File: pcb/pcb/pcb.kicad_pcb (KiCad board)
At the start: 2 copper layers, 66 x 40.6 mm, 14 parts, among them J1 UART, J2 Barrel_Jack, J3 Stepper, U1 ESP32-WROOM-32, U2 TSR_1-2433

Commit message: Route pcb
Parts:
- added H1: MountingHole, MountingHole:MountingHole_2.7mm_M2.5_Pad, F.Cu at (182.9, 76.2)
- added H2: MountingHole, MountingHole:MountingHole_2.5mm_Pad, F.Cu at (241.3, 76.2)
- added H3: MountingHole, MountingHole:MountingHole_2.5mm_Pad, F.Cu at (182.9, 109.2)
- added H4: MountingHole, MountingHole:MountingHole_2.5mm_Pad, F.Cu at (241.3, 109.2)
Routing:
- net GND: track 0.00 -> 148.7 mm
- net +12V: track 0.00 -> 50.2 mm
- net +3V3: track 0.00 -> 46.0 mm, vias 0 -> 1
- net /SLP: track 0.00 -> 44.2 mm
- net /DIR: track 0.00 -> 40.8 mm
- net /STEP: track 0.00 -> 38.8 mm
- net Net-(C1-Pad1): track 0.00 -> 34.1 mm, vias 0 -> 2
- net /B2: track 0.00 -> 31.7 mm
- net /B1: track 0.00 -> 31.7 mm
- net /A1: track 0.00 -> 31.0 mm
- net /A2: track 0.00 -> 30.2 mm
- net /RX: track 0.00 -> 17.2 mm
- net /TX: track 0.00 -> 8.45 mm
- net Net-(C6-Pad1): track 0.00 -> 6.42 mm
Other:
- outline, holes or cut-outs redrawn

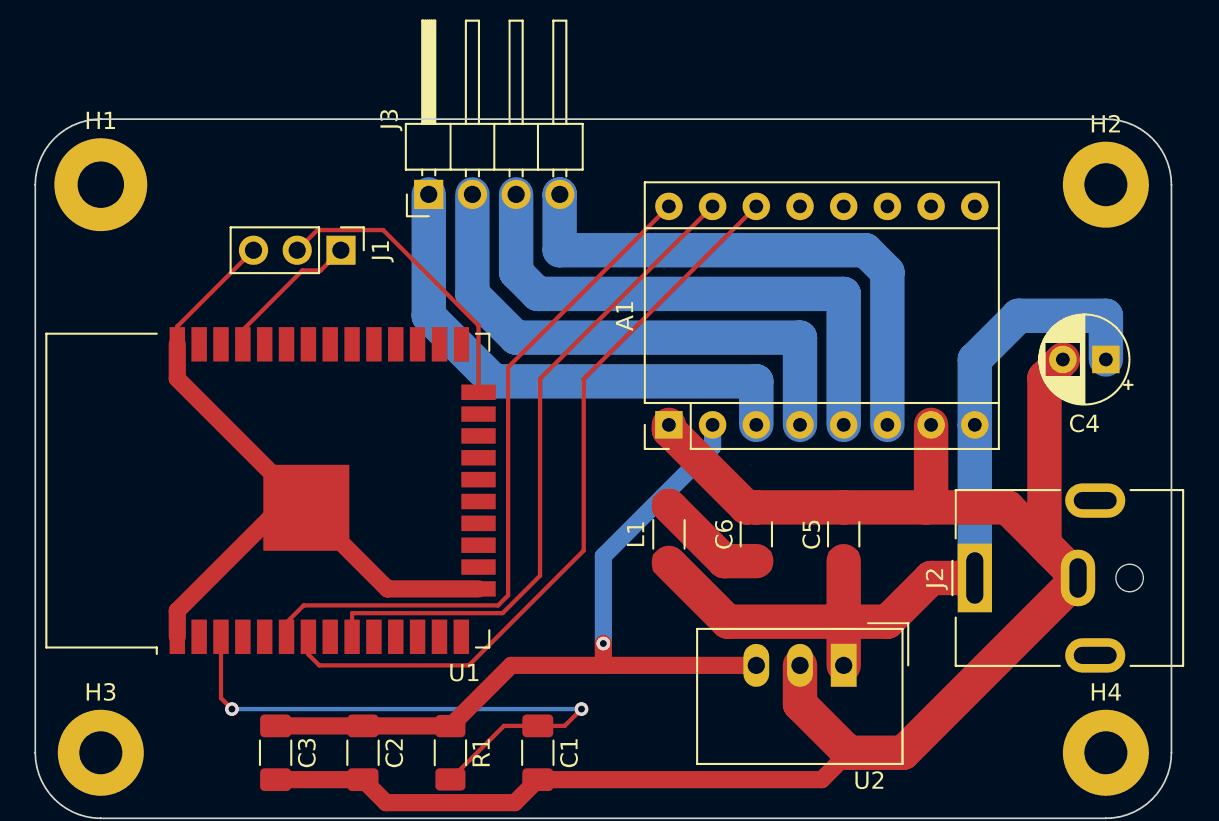
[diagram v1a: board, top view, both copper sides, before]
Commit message: Add silkscreen
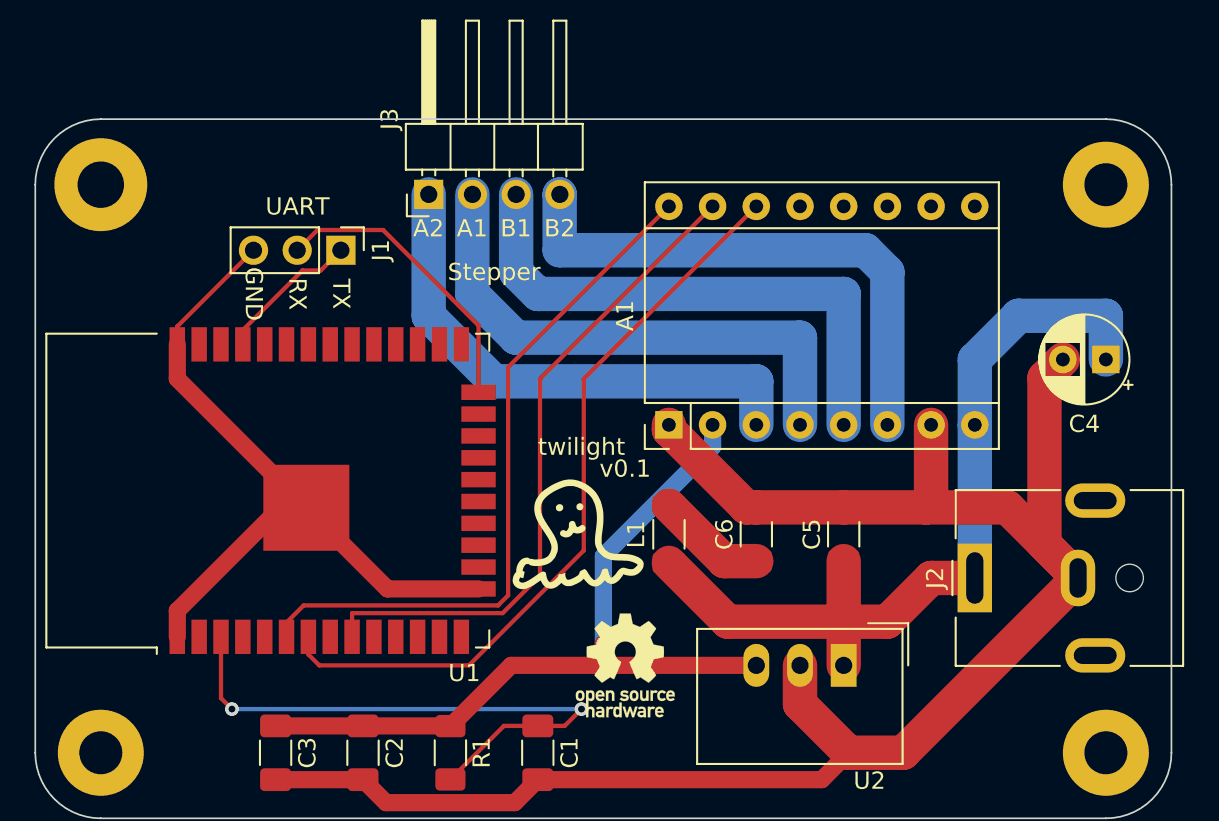
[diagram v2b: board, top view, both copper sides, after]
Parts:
- added G***: LOGO, CustomSymbols:octo, F.Cu at (210.8, 96.5)
- added REF**: OSHW-Logo_5.7x6mm_SilkScreen, Symbol:OSHW-Logo_5.7x6mm_SilkScreen, F.Cu at (213.4, 104.1)
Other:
- board text added: "A1"
- board text added: "A2"
- board text added: "B1"
- board text added: "B2"
- board text added: "GND"
- board text added: "RX"
- board text added: "Stepper"
- board text added: "TX"
- board text added: "UART"
- board text added: "twilight"
- board text added: "v0.1"

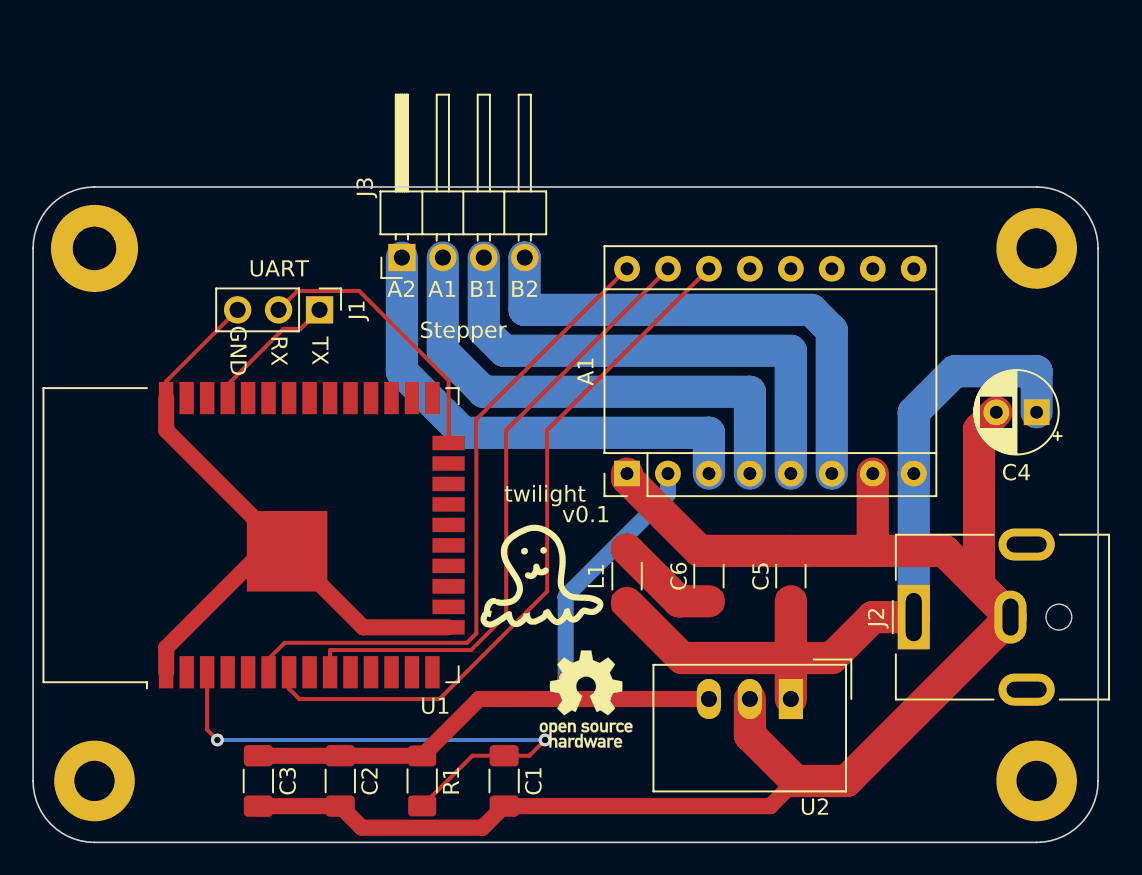
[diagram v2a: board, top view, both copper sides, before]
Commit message: add reset and boot buttons
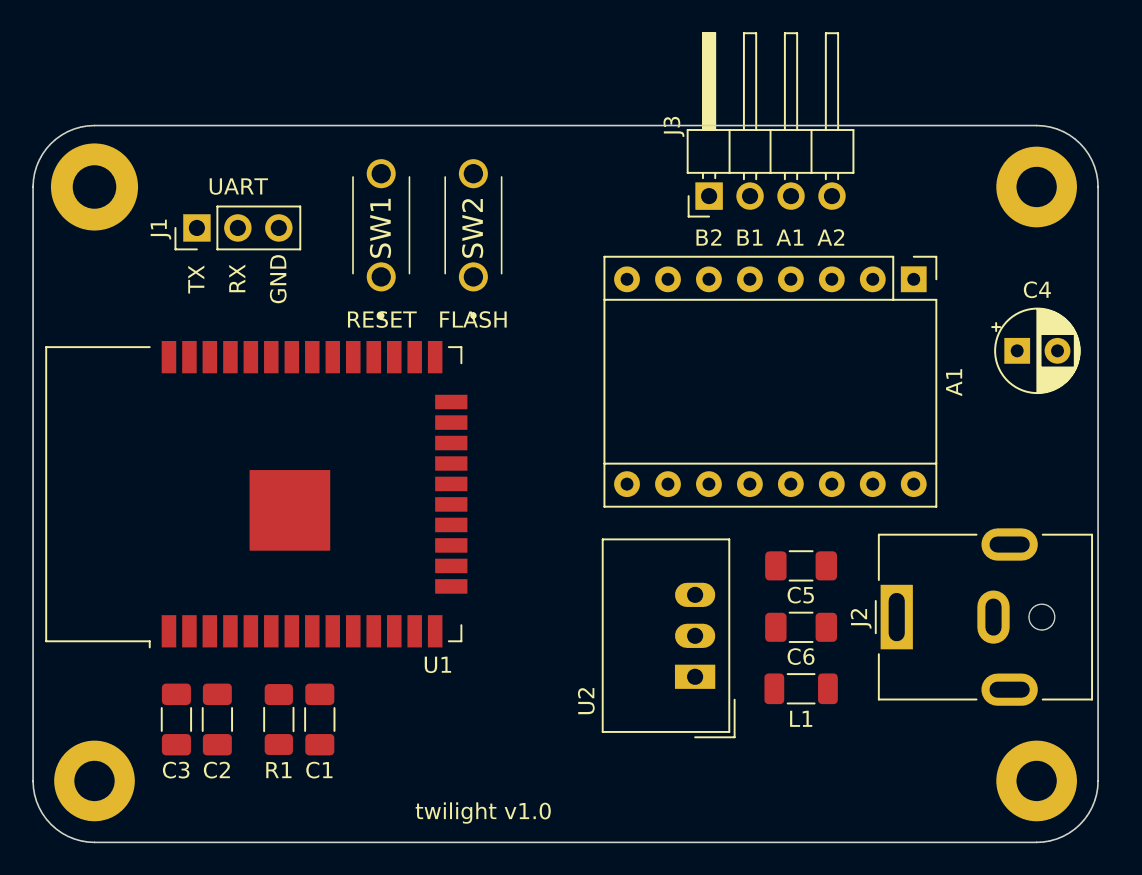
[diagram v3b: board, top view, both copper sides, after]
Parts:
- removed G***: LOGO, CustomSymbols:octo
- removed REF**: OSHW-Logo_5.7x6mm_SilkScreen, Symbol:OSHW-Logo_5.7x6mm_SilkScreen
- added SW1: RESET, buttons:PTS636SK43LFS, F.Cu at (200.7, 78.0)
- added SW2: FLASH, buttons:PTS636SK43LFS, F.Cu at (206.4, 78.0)
- C1: value 1uF -> 0.1uF
- moved A1 21.5 mm to (233.7, 78.1), turned to -90 degrees
- moved J3 19.4 mm to (221.0, 73.0)
- moved L1 12.9 mm to (226.7, 103.5), turned to 180 degrees
- moved C1 12.0 mm to (196.8, 105.4), turned to 90 degrees
- moved R1 9.67 mm to (194.3, 105.4)
- moved J1 9.15 mm to (189.2, 74.9), turned to 90 degrees
- moved C2 8.52 mm to (190.5, 105.4)
- moved C6 6.54 mm to (226.7, 99.7), turned to 180 degrees
- moved C3 6.35 mm to (188.0, 105.4)
- moved U2 6.10 mm to (220.1, 102.8), turned to 90 degrees
- moved C4 4.00 mm to (240.1, 82.5), turned to 0 degrees
- moved H1 3.81 mm to (182.9, 72.4)
- moved H2 3.81 mm to (241.3, 72.4)
- moved U1 2.55 mm to (195.8, 91.4)
- moved J2 1.06 mm to (232.6, 99.1)
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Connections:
- J3 pad 1: /A2 -> /B2
- J3 pad 2: /A1 -> /B1
- J3 pad 3: /B1 -> /A1
- J3 pad 4: /B2 -> /A2
- U1 pad 24: /RX -> unconnected-(U1-Pad24)
- U1 pad 25: unconnected-(U1-Pad25) -> IO0
- U1 pad 34: unconnected-(U1-Pad34) -> /RX
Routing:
- net GND: track 148.7 -> 0.00 mm
- net +12V: track 50.2 -> 0.00 mm
- net +3V3: track 46.0 -> 0.00 mm, vias 1 -> 0
- net /SLP: track 44.2 -> 0.00 mm
- net /DIR: track 40.8 -> 0.00 mm
- net /STEP: track 38.8 -> 0.00 mm
- net Net-(C1-Pad1): track 34.1 -> 0.00 mm, vias 2 -> 0
- net /B2: track 31.7 -> 0.00 mm
- net /B1: track 31.7 -> 0.00 mm
- net /A1: track 31.0 -> 0.00 mm
- net /A2: track 30.2 -> 0.00 mm
- net /RX: track 17.2 -> 0.00 mm
- net /TX: track 8.45 -> 0.00 mm
- net Net-(C6-Pad1): track 6.42 -> 0.00 mm
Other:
- board size 66 x 40.6 mm -> 66 x 44.5 mm
- board text added: "FLASH"
- board text added: "RESET"
- board text added: "twilight v1.0"
- board text removed: "Stepper"
- board text removed: "twilight"
- board text removed: "v0.1"

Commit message: route traces
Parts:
- moved C4 133.3 mm to (111.2, 48.9)
- moved H2 112.0 mm to (132.1, 47.6)
- moved H4 112.0 mm to (132.1, 84.4)
- moved J2 112.0 mm to (123.4, 74.3)
- moved C6 111.6 mm to (118.3, 73.0)
- moved C5 111.1 mm to (117.1, 78.1), turned to 90 degrees
- moved SW2 110.1 mm to (99.1, 53.2)
- moved U2 110.1 mm to (112.8, 78.0)
- moved L1 110.1 mm to (119.6, 78.1), turned to 90 degrees
- moved C1 107.7 mm to (92.1, 80.6), turned to 0 degrees
- moved J3 106.4 mm to (117.5, 48.2)
- moved C2 106.4 mm to (87.0, 80.6), turned to 180 degrees
- moved A1 106.3 mm to (130.2, 54.0)
- moved R1 105.8 mm to (92.1, 78.1), turned to 180 degrees
- moved C3 104.6 mm to (87.0, 78.1), turned to 180 degrees
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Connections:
- net Net-(C1-Pad1) renamed /EN
- U1 pad 12: unconnected-(U1-Pad12) -> /DIR
- U1 pad 13: unconnected-(U1-Pad13) -> /STEP
- U1 pad 14: unconnected-(U1-Pad14) -> /SLP
- U1 pad 6: /DIR -> unconnected-(U1-Pad6)
- U1 pad 7: /SLP -> unconnected-(U1-Pad7)
- U1 pad 9: /STEP -> unconnected-(U1-Pad9)
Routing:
- net GND: track 0.00 -> 154.2 mm
- net +3V3: track 0.00 -> 84.3 mm, vias 0 -> 2
- net +12V: track 0.00 -> 57.4 mm
- net /DIR: track 0.00 -> 38.9 mm
- net /EN: track 0.00 -> 38.7 mm
- net /STEP: track 0.00 -> 34.6 mm
- net /SLP: track 0.00 -> 28.8 mm
- net /TX: track 0.00 -> 8.87 mm
- net /RX: track 0.00 -> 8.34 mm
- net IO0: track 0.00 -> 6.36 mm
- net /B2: track 0.00 -> 5.81 mm
- net /B1: track 0.00 -> 5.81 mm
- net /A2: track 0.00 -> 5.81 mm
- net /A1: track 0.00 -> 5.81 mm
- net Net-(C6-Pad1): track 0.00 -> 3.54 mm
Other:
- board size 66 x 44.5 mm -> 58.4 x 44.4 mm
